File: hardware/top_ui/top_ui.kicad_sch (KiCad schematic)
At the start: 24 parts, among them J1 USB-C, J2 J_STK_A, J3 J_STK_B, J5 ST77916 QSPI, J6 Stern, J7 Radar, Q1 BC847, Q2 P-FET 20V 1A, SW1A BTN1, SW1B BTN1, SW2A BTN2, SW2B BTN2, SW3A BTN3, SW3B BTN3, SW4A BTN4, SW4B BTN4, U1 USBLC6-2SC6, U2 SHT40-AD1B

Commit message: feat: Layouts aller drei Boards - platziert, vernetzt, DRC-sauber
Neuer Generator tools/gen_layouts.py erzeugt die drei .kicad_pcb komplett:
Outline, Bohrbild, Frontmarkierung, Antennen-Sperrflaeche, alle Footprints
mit Netzen aus den Schaltplan-Generatoren, PGND-Zonen beidseitig. Mechanisch
gebundene Teile exakt platziert (Stackverbinder deckungsgleich, Taster auf
den Sichel-Stoesselpositionen, USB-C am Rand, ESP32-Antenne an der
Frontkante, FET-Raster berechnet); Rest kollisionsfrei per Spiralsuche mit
Netznachbar-Heuristik. DRC (pcbnew.WriteDRCReport - kicad-cli kann das erst
ab KiCad 8): KEINE Platzierungsfehler auf allen drei Boards. Offen bleibt
das ROUTING - die Boards sind route-fertig, Leiterbahnen sind Handarbeit.

Die Kollisionspruefung fand einen echten Mechanikfehler: Bohrbild v2.
Die Bohrungen 120/240 Grad lagen ~2 mm neben den Sicheltasten-Stoesseln
(117/243) - Schraubenkopf trifft Taster. Auf r21,5 blockieren Stack-
verbinder, ESP32-Antenne und Leistungsstecker alle uebrigen Winkel; frei
sind exakt 0/180. Jetzt zwei Schrauben, Verdrehsicherung ueber die beiden
Stackverbinder. docs/04 und gen_boards nachgezogen.

Weitere Ausbeute der Iterationen (jede von DRC oder Kollisionspruefung
erzwungen): Stackverbinder auf x=+/-14,2 (Diagonaltaster!), Taster auf
Alps-SKRK-Footprint (EVQP2-Pads ragten 0,1 mm an den Rand), Rotations-
automatik fuer die Taster nach minimalem Pad-Radius, Sicherung auf
SMD-NANO2, Bulk-Elkos niedrigbauend auf die Rueckseite, Treiber gestaffelt
unter den FETs, HSOP ohne Thermal-Vias (0,2-mm-Bohrungen), Flip-Bug der
Autoplatzierung (Teile blieben nach B-Versuch gespiegelt), Segfault-
Workarounds fuer ZONE_FILLER und BOX2-Merge in der headless pcbnew-API.

Schaltplan-Nebenkorrekturen: L78L12-Pinbelegung war verdreht (1=OUT!),
Q1-Verpolschutz auf PowerPAK mit eigener Pad-Zuordnung, SHT4x-Footprint
lag in Sensor_Humidity statt Package_DFN_QFN.

USB-C-Randverletzungen (10) sind als Steckerueberhang beabsichtigt und
werden getrennt ausgewie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
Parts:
- SW1A, SW1B, SW2A, SW2B, SW3A, SW3B, SW4A, SW4B: footprint Button_Switch_SMD:SW_SPST_EVQP2 -> Button_Switch_SMD:SW_Push_SPST_NO_Alps_SKRK; MPN niedrig, 3,9x2,9 - Position siehe mechanical/frontplate.py -> Alps SKRK o.ae., 3,9x2,9, Pads laengs - Position siehe mech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
- U2: footprint Package_DFN_QFN:DFN-4-1EP_1.5x1.5mm_P0.8mm_EP0.7x0.9mm -> Sensor_Humidity:Sensirion_DFN-4_1.5x1.5mm_P0.8mm_SHT4x_NoCentralPad
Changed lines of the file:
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@@
     (property "Value" "BTN1" (at 234.9500 20.3200 0)
       (effects (font (size 1.27 1.27)) (justify left)))
-    (property "Footprint" "Button_Switch_SMD:SW_SPST_EVQP2" (at 228.6000 25.4000 0)
+    (property "Footprint" "Button_Switch_SMD:SW_Push_SPST_NO_Alps_SKRK" (at 228.6000 25.4000 0)
       (effects (font (size 1.27 1.27)) hide))
-    (property "MPN" "niedrig, 3,9x2,9 - Position siehe mechanical/frontplate.py" (at 228.6000 27.9400 0)
+    (property "MPN" "Alps SKRK o.ae., 3,9x2,9, Pads laengs - Position siehe mechanical/frontplate.py" (at 228.6000 27.9400 0)
       (effects (font (size 1.27 1.27)) hide))
     (pin "1")
@@
     (property "Value" "BTN1" (at 285.7500 20.3200 0)
       (effects (font (size 1.27 1.27)) (justify left)))
-    (property "Footprint" "Button_Switch_SMD:SW_SPST_EVQP2" (at 279.4000 25.4000 0)
+    (property "Footprint" "Button_Switch_SMD:SW_Push_SPST_NO_Alps_SKRK" (at 279.4000 25.4000 0)
       (effects (font (size 1.27 1.27)) hide))
-    (property "MPN" "niedrig, 3,9x2,9 - Position siehe mechanical/frontplate.py" (at 279.4000 27.9400 0)
+    (property "MPN" "Alps SKRK o.ae., 3,9x2,9, Pads laengs - Position siehe mechanical/frontplate.py" (at 279.4000 27.9400 0)
       (effects (font (size 1.27 1.27)) hide))
     (pin "1")
@@
     (property "Value" "BTN2" (at 336.5500 20.3200 0)
       (effects (font (size 1.27 1.27)) (justify left)))
-    (property "Footprint" "Button_Switch_SMD:SW_SPST_EVQP2" (at 330.2000 25.4000 0)
+    (property "Footprint" "Button_Switch_SMD:SW_Push_SPST_NO_Alps_SKRK" (at 330.2000 25.4000 0)
       (effects (font (size 1.27 1.27)) hide))
-    (property "MPN" "niedrig, 3,9x2,9 - Position siehe mechanical/frontplate.py" (at 330.2000 27.9400 0)
+    (property "MPN" "Alps SKRK o.ae., 3,9x2,9, Pads laengs - Position siehe mechanical/frontplate.py" (at 330.2000 27.9400 0)
       (effects (font (size 1.27 1.27)) hide))
     (pin "1")
@@
     (property "Value" "BTN2" (at 387.3500 20.3200 0)
       (effects (font (size 1.27 1.27)) (justify left)))
-    (property "Footprint" "Button_Switch_SMD:SW_SPST_EVQP2" (at 381.0000 25.4000 0)
+    (property "Footprint" "Button_Switch_SMD:SW_Push_SPST_NO_Alps_SKRK" (at 381.0000 25.4000 0)
       (effects (font (size 1.27 1.27)) hide))
-    (property "MPN" "niedrig, 3,9x2,9 - Position siehe mechanical/frontplate.py" (at 381.0000 27.9400 0)
+    (property "MPN" "Alps SKRK o.ae., 3,9x2,9, Pads laengs - Position siehe mechanical/frontplate.py" (at 381.0000 27.9400 0)
       (effects (font (size 1.27 1.27)) hide))
     (pin "1")
@@
     (property "Value" "BTN3" (at 438.1500 20.3200 0)
       (effects (font (size 1.27 1.27)) (justify left)))
-    (property "Footprint" "Button_Switch_SMD:SW_SPST_EVQP2" (at 431.8000 25.4000 0)
+    (property "Footprint" "Button_Switch_SMD:SW_Push_SPST_NO_Alps_SKRK" (at 431.8000 25.4000 0)
       (effects (font (size 1.27 1.27)) hide))
-    (property "MPN" "niedrig, 3,9x2,9 - Position siehe mechanical/frontplate.py" (at 431.8000 27.9400 0)
+    (property "MPN" "Alps SKRK o.ae., 3,9x2,9, Pads laengs - Position siehe mechanical/frontplate.py" (at 431.8000 27.9400 0)
       (effects (font (size 1.27 1.27)) hide))
     (pin "1")
@@
     (property "Value" "BTN3" (at 31.7500 64.7700 0)
       (effects (font (size 1.27 1.27)) (justify left)))
-    (property "Footprint" "Button_Switch_SMD:SW_SPST_EVQP2" (at 25.4000 69.8500 0)
+    (property "Footprint" "Button_Switch_SMD:SW_Push_SPST_NO_Alps_SKRK" (at 25.4000 69.8500 0)
       (effects (font (size 1.27 1.27)) hide))
-    (property "MPN" "niedrig, 3,9x2,9 - Position siehe mechanical/frontplate.py" (at 25.4000 72.3900 0)
+    (property "MPN" "Alps SKRK o.ae., 3,9x2,9, Pads laengs - Position siehe mechanical/frontplate.py" (at 25.4000 72.3900 0)
       (effects (font (size 1.27 1.27)) hide))
     (pin "1")
@@
     (property "Value" "BTN4" (at 82.5500 64.7700 0)
       (effects (font (size 1.27 1.27)) (justify left)))
-    (property "Footprint" "Button_Switch_SMD:SW_SPST_EVQP2" (at 76.2000 69.8500 0)
+    (property "Footprint" "Button_Switch_SMD:SW_Push_SPST_NO_Alps_SKRK" (at 76.2000 69.8500 0)
       (effects (font (size 1.27 1.27)) hide))
-    (property "MPN" "niedrig, 3,9x2,9 - Position siehe mechanical/frontplate.py" (at 76.2000 72.3900 0)
+    (property "MPN" "Alps SKRK o.ae., 3,9x2,9, Pads laengs - Position siehe mechanical/frontplate.py" (at 76.2000 72.3900 0)
       (effects (font (size 1.27 1.27)) hide))
     (pin "1")
@@
     (property "Value" "BTN4" (at 133.3500 64.7700 0)
       (effects (font (size 1.27 1.27)) (justify left)))
-    (property "Footprint" "Button_Switch_SMD:SW_SPST_EVQP2" (at 127.0000 69.8500 0)
+    (property "Footprint" "Button_Switch_SMD:SW_Push_SPST_NO_Alps_SKRK" (at 127.0000 69.8500 0)
       (effects (font (size 1.27 1.27)) hide))
-    (property "MPN" "niedrig, 3,9x2,9 - Position siehe mechanical/frontplate.py" (at 127.0000 72.3900 0)
+    (property "MPN" "Alps SKRK o.ae., 3,9x2,9, Pads laengs - Position siehe mechanical/frontplate.py" (at 127.0000 72.3900 0)
       (effects (font (size 1.27 1.27)) hide))
     (pin "1")
@@
     (property "Value" "SHT40-AD1B" (at 184.1500 64.7700 0)
       (effects (font (size 1.27 1.27)) (justify left)))
-    (property "Footprint" "Package_DFN_QFN:DFN-4-1EP_1.5x1.5mm_P0.8mm_EP0.7x0.9mm" (at 177.8000 69.8500 0)
+    (property "Footprint" "Sensor_Humidity:Sensirion_DFN-4_1.5x1.5mm_P0.8mm_SHT4x_NoCentralPad" (at 177.8000 69.8500 0)
       (effects (font (size 1.27 1.27)) hide))
     (property "MPN" "Adresse 0x44 - muss zur YAML passen; thermisch vom Board entkoppeln (Schlitze)" (at 177.8000 72.3900 0)

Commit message: Reed-Kontakte, Haubenkontakt, Klinkenbuchse, ToF statt Radar
Funktional neu
--------------
- Zwei Reed-Eingaenge fuer Fensterkontakte auf den einzigen noch freien
  Expanderpins P6/P7. 10k Pullup, 1k Serie, 100n und TVS je Kanal; bei
  geschlossenem Kontakt liegen 0,3 V am PCF8574, sicher unter VIL.
- Meldekontakt zur Dunstabzugshaube ueber PhotoMOS AQY282GS statt Relais:
  potentialfrei, 60 V / 0,8 A, kein Spulenstrom, keine Bauhoehe im 9-mm-
  Stapelspalt. NUR SELV - bei 230 V gehoert das Schaltglied nicht in die Dose.
- Weihnachtsstern jetzt gesteckt: Klinkenbuchse im oberen Steg der
  Frontplatte, PTC 0,2 A direkt an der Buchse gegen den Kurzschluss beim
  Stecken, Bulk vor die Sicherung gelegt.
- Radar durch VL53L1X (ToF) ersetzt. Hinter dieser Frontplatte hat kein
  20-mm-Radarmodul freie Sicht; der ToF passt als 4,9 x 2,5 mm grosser Chip
  in den Steg. Er misst Entfernung statt Empfindlichkeit - Schwelle exakt
  1 m - und deckt in der Fensterlaibung zugleich den Durchstieg ab.
  Netze umbenannt: RADAR_INT -> PRESENCE_INT, UART_RADAR_* -> UART_AUX_*.
  J7 bleibt unbestueckt als Reserve, damit das Stackpinout unberuehrt bleibt.

Frontplatte
-----------
Oberer Steg 9 -> 17 mm, damit Klinkenbuchse und ToF-Fenster nebeneinander
passen; Sicheln dadurch ~70 -> ~45 Grad, Stoesselwinkel 18 -> 12 Grad.
ToF-Kanal konisch (4,5 vorn, 3,0 hinten) fuer den Sichtkegel. Kabelausgang
Ø4,5 entfaellt. Selbsttests bestanden, STEP/STL neu erzeugt.

KiCad 10
--------
Die Generatoren liefen nur gegen KiCad-9-Bibliotheken. Migriert:
- Symbol- und Footprintpfad werden gefunden (Linux, macOS, Umgebungsvariable)
- PCF8574 -> PCF8574T (pinkompatibel, als Alias)
- Q_NMOS_GDS/Q_PMOS_GSD/Q_NPN_BCE liegen jetzt als hardware/lib/
  SwitchStack.kicad_sym im Projekt. KiCad 10 nummeriert die Stockvarianten
  mit G/D/S bzw. B/C/E - ein Alias haette die Anschluesse still vertauscht.
- USB-C-Schirm heisst SH statt S1, Zonen-API SetDoNotAllowZoneFills,
  DRC laeuft ueber kicad-cli statt WriteDRCRepo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
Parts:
- added C3: 100n, Capacitor_SMD:C_0603_1608Metric, symbol Device:C
- added C4: 4u7, Capacitor_SMD:C_0603_1608Metric, symbol Device:C
- added F1: 0,2 A PTC, Fuse:Fuse_1206_3216Metric, symbol Device:Polyfuse
- added R5: 10k, Resistor_SMD:R_0603_1608Metric, symbol Device:R
- added U3: VL53L1X, Sensor_Distance:ST_VL53L1x, symbol Sensor_Distance:VL53L1CXV0FY1
- J6: value Stern -> Stern Klinke; footprint Connector_JST:JST_PH_B2B-PH-K_1x02_P2.00mm_Vertical -> Connector_Audio:Jack_3.5mm_QingPu_WQP-PJ398SM_Vertical_CircularHoles; symbol Connector_Generic:Conn_01x02 -> Connector_Audio:AudioJack2_SwitchT; MPN Kabel durch den Frontplatten-Ausgang Ø4,5 -> PLATZHALTER 3,5 mm vertikal - Zielteil 2,5 mm, Bauhoehe max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
- J7: value Radar -> Reserve UART; MPN Belegung an reales Modul anpassen (offener Punkt 17) -> DNP - Reserve fuer ein Satellitenmodul
- Q1: symbol Device:Q_NPN_BCE -> SwitchStack:Q_NPN_BCE
- Q2: symbol Device:Q_PMOS_GSD -> SwitchStack:Q_PMOS_GSD
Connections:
- net 3V3_SYS: now also C3.1, C4.1, R5.1, U3.1 (AVDDVCSEL), U3.11 (AVDD)
- net I2C_SCL: now also U3.10 (SCL)
- net I2C_SDA: now also U3.9 (SDA)
- net PGND: now also J1.SH (SHIELD), J6.S, C3.2, C4.2, U3.12 (GND), U3.2 (AVSSVCSEL), U3.3 (GND), U3.4 (GND), U3.6 (GND); no longer J1.S1 (SHIELD), J6.2 (Pin_2)
- net STAR_OUT: now also J6.T, F1.2; no longer C2.1, J6.1 (Pin_1)
- net RADAR_INT renamed PRESENCE_INT
- net PRESENCE_INT: now also U3.7 (GPIO1)
- net UART_RADAR_RX renamed UART_AUX_RX
- net UART_RADAR_TX renamed UART_AUX_TX
- new net STAR_SW: C2.1, F1.1
- new net TOF_XSHUT: R5.2, U3.5 (XSHUT)
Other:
- moved on the sheet: J2, J3, J7

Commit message: Weg A umgesetzt: Top-Board quadratisch, vier Ecktaster unter den Kreuzen
Umriss
------
gen_layouts.py und gen_boards.py kennen jetzt eine zweite Kontur. Das Top-Board
ist ein abgerundetes Quadrat, 49 x 49 mm mit Eckradius 4 - vier Geraden und vier
Boegen auf Edge.Cuts. Mid und Bottom bleiben rund und unangetastet; ihre
Boarddateien wurden nicht angefasst, die 985 Leiterbahnen des Bottom-Boards sind
unberuehrt.

Kantenmitte 24,5 liegt 0,5 mm innerhalb der Rastnasenlinie der Zentralscheibe
(50,0). Der Konturtest der Platzierung (inside_outline) rechnet die abgerundeten
Ecken korrekt mit, sonst haette die Automatik die Ecken verschenkt.

Taster
------
Acht parallelgeschaltete Sicheltaster werden vier Ecktaster, exakt auf
(+/-18,0 / +/-20,0) - den gemessenen Druckkreuzen der Scheibe. Ein Kreuz ist
3,2 mm gross und trifft genau einen Taster; parallelschalten waere sinnlos.
Der Schaltplan ist entsprechend neu erzeugt (25 statt 29 Bauteile,
Netzlistenvergleich bestanden), die Stuecklisten ebenfalls.

Durchbrueche
------------
Die vier Oeffnungen der Scheibe liegen jetzt bei (+/-9 / +/-19) - in den
Diagonalfeldern zwischen Pfeil und Ecktaster, mit rund 8 mm Abstand zu beiden.
Auf den Diagonalen selbst ist kein Platz mehr, dort sitzen die Kreuze. Links
oben ToF, links unten Klinke, rechts zweimal Lueftung - und weil dort die Luft
hereinkommt, sitzt der SHT4x jetzt unter dem oberen rechten Schlitz (Punkt 46).

Ergebnis: Platzierung kollisionsfrei, DRC unveraendert 28 clearance (die
bekannten Pad-Abstaende im USB-C-Footprint) plus die eine Randverletzung des
Klinken-Platzhalters.

Was dabei aufgefallen ist
-------------------------
gen_boards.py ueberschreibt hardware/<slug>/<slug>.kicad_pcb - es haette beim
naechsten Lauf die Bestueckung UND die Leiterbahnen aller drei Boards
weggeworfen. Das steht jetzt als Warnung im Docstring.

Der Fertigungsnutzen ist geloescht: gen_panel.py setzt drei Kreise Oe52
nebeneinander und wuerde um das quadratische Board eine runde Fraesbahn leg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
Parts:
- removed SW1A, SW1B: BTN1, Button_Switch_SMD:SW_Push_SPST_NO_Alps_SKRK, symbol Switch:SW_Push
- removed SW2A, SW2B: BTN2, Button_Switch_SMD:SW_Push_SPST_NO_Alps_SKRK, symbol Switch:SW_Push
- removed SW3A, SW3B: BTN3, Button_Switch_SMD:SW_Push_SPST_NO_Alps_SKRK, symbol Switch:SW_Push
- removed SW4A, SW4B: BTN4, Button_Switch_SMD:SW_Push_SPST_NO_Alps_SKRK, symbol Switch:SW_Push
- added SW1: BTN1, Button_Switch_SMD:SW_Push_SPST_NO_Alps_SKRK, symbol Switch:SW_Push
- added SW2: BTN2, Button_Switch_SMD:SW_Push_SPST_NO_Alps_SKRK, symbol Switch:SW_Push
- added SW3: BTN3, Button_Switch_SMD:SW_Push_SPST_NO_Alps_SKRK, symbol Switch:SW_Push
- added SW4: BTN4, Button_Switch_SMD:SW_Push_SPST_NO_Alps_SKRK, symbol Switch:SW_Push
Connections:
- net BTN1: now also SW1.1
- net BTN2: now also SW2.1
- net BTN3: now also SW3.1
- net BTN4: now also SW4.1
- net PGND: now also SW1.2, SW2.2, SW3.2, SW4.2
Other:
- moved on the sheet: C1, C2, C3, C4, F1, J2, J3, J5, J6, J7, Q1, Q2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

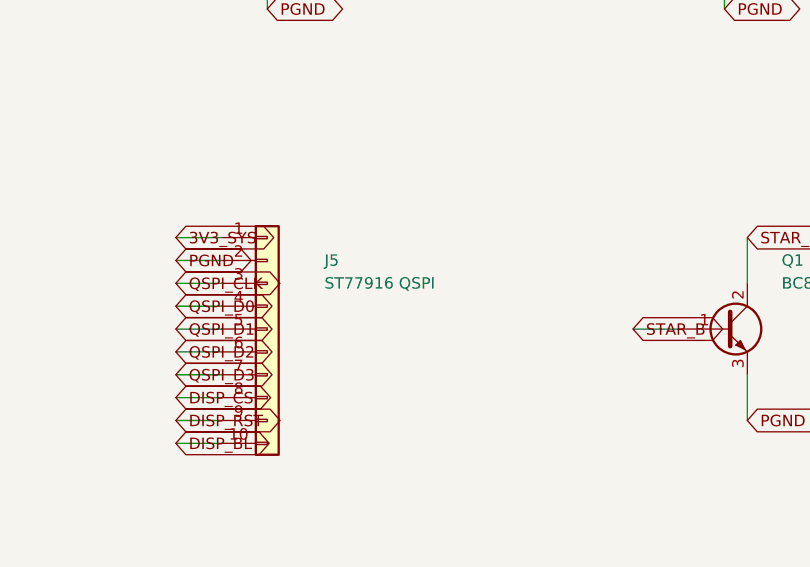
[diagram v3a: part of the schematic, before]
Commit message: Display auf ST7789 240x280 umgestellt; Tastenpaare in der Firmware aufgeloest
Display
-------
Der Fensterausschnitt der Zentralscheibe misst gemessene 32,70 x 27,00 mm. Die
aktive Flaeche eines 1,69-Zoll-Panels mit 240x280 ist quer eingebaut
32,63 x 27,97 - in der Breite bleiben 0,07 mm, in der Hoehe verdeckt das Fenster
einen halben Millimeter je Seite. Damit ist Punkt 43 entschieden.

Der Gewinn liegt nicht in der Groesse, sondern im Treiber: ESPHome kennt den
ST7789 nativ. st77916_init.yaml mit seinen 214 Herstellerkommandos ist geloescht.

Die Netznamen am Stack bleiben QSPI_*, obwohl der ST7789 4-Draht-SPI ist. Sie
laufen ueber J_STK_B durch alle drei Boards, und eine Umbenennung wuerde auch
den Bottom-Schaltplan aendern - dessen Layout traegt 985 Leiterbahnen. Die
Belegung steht stattdessen als Kommentar an beiden Stellen: QSPI_CLK = SCK,
QSPI_D0 = MOSI, QSPI_D1 = DC, D2/D3 frei.

Tastenpaare
-----------
Die vier Ecktaster heissen in der Konfiguration jetzt ecke_ol/or/ul/ur und sind
intern - einzeln bedeuten sie nichts. Darueber liegen vier Template-Sensoren,
die die Paare aufloesen: hoch = ol+or, runter = ul+ur, OK = or+ur, play = ol+ul.
30 ms Verzoegerung fangen ab, dass die beiden Taster eines Paares nie exakt
gleichzeitig schliessen.

Die Zuordnung Richtung -> Aktion ist vorlaeufig (hoch/runter fahren beide
Jalousien, OK stoppt, play liegt brach). Verbindlich wird sie erst mit der
Menue-Zustandsmaschine, Punkt 37.

Ehrlich dazu
------------
Die Konfiguration ist NICHT mit `esphome config` geprueft - auf diesem Rechner
ist ESPHome nicht installiert. Sie parst als YAML, mehr ist nicht gezeigt.
Besonders die Panel-Offsets (0/20) und die Template-Lambdas gehoeren vor dem
ersten Flash validiert. Der Hinweis steht in der Datei selbst, in
firmware/README, in der README und in docs/13.

Co-Authored-By: Claude Opus 5 (1M context) <noreply@anthropic.com>
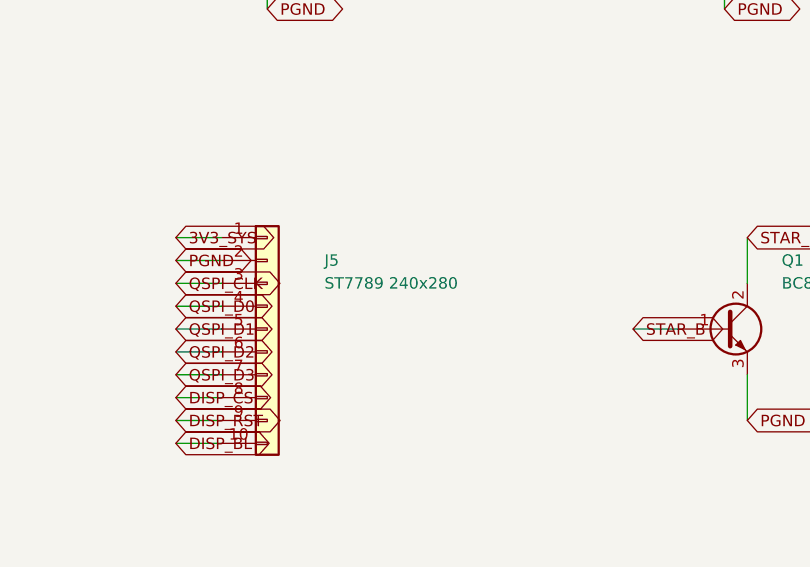
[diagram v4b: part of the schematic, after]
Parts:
- J5: value ST77916 QSPI -> ST7789 240x280; MPN PLATZHALTER - reales Modul-FPC vermessen, dann Footprint ta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 -> PLATZHALTER - reales Modul mit FPC vermessen, dann Footprin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
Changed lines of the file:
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@@
     (property "Reference" "J5" (at 82.5500 62.2300 0)
       (effects (font (size 1.27 1.27)) (justify left)))
-    (property "Value" "ST77916 QSPI" (at 82.5500 64.7700 0)
+    (property "Value" "ST7789 240x280" (at 82.5500 64.7700 0)
       (effects (font (size 1.27 1.27)) (justify left)))
     (property "Footprint" "Connector_PinHeader_1.27mm:PinHeader_1x10_P1.27mm_Vertical" (at 76.2000 69.8500 0)
       (effects (font (size 1.27 1.27)) hide))
-    (property "MPN" "PLATZHALTER - reales Modul-FPC vermessen, dann Footprint tauschen" (at 76.2000 72.3900 0)
+    (property "MPN" "PLATZHALTER - reales Modul mit FPC vermessen, dann Footprint und Pinzahl tauschen (Module haben meist 8 Pins)" (at 76.2000 72.3900 0)
       (effects (font (size 1.27 1.27)) hide))
     (pin "1")

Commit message: Stehende USB-C-Buchse, Nutzen mit gemischter Geometrie - Top ist DRC-sauber
USB-C (Punkt 45)
----------------
Gewaehlt: G-Switch GT-USB-7051x, vertikal SMT, 22 Pads (A- und B-Reihe
vollstaendig, also steckrichtungsunabhaengig), Footprint 9,94 x 6,40 mm,
LCSC C2843970. Sie sitzt mittig oben, zeigt nach vorn und liegt unter der
Zentralscheibe - erreichbar erst nach deren Abnahme, so wie es Punkt 45
verlangt.

Der Nebeneffekt ist der eigentliche Gewinn: Die 28 clearance-Meldungen, die das
Top-Board seit dem ersten Layout begleitet haben, sind verschwunden. Sie waren
nie ein Layoutfehler, sondern die zu eng gerasterten Pads der liegenden GCT
USB4085 gegen unsere 0,15-mm-Vorgabe. Das Top-Board meldet jetzt KEINEN
DRC-Fehler mehr - nur noch drei bewusste Randverletzungen (zwei davon sind die
NPTH-Loecher der Buchse gegen ihre eigenen Pads, eine der Klinken-Platzhalter).

Der Waiver-Mechanismus in gen_layouts.py war dafuer zu grob: Er hat nur auf das
Zeilenende geprueft. Jetzt wird nur gewaivert, wenn ALLE in der Meldung
genannten Bauteile in der Ausnahmeliste stehen - sonst verschluckt ein Waiver
fuer J1 auch eine echte Kollision J1 gegen U3.

Fertigungsnutzen
----------------
gen_panel.py beherrscht gemischte Geometrie: zwei Kreise Oe52 und ein
abgerundetes Quadrat 47 x 47. Das Quadrat bekommt seine Fraesfuge als
Parallelkurve der Kontur, mit vier Stegen - je einer pro Kante, um 10 mm aus der
Mitte versetzt, weil dort entweder eine Befestigungsbohrung oder der
ueberstehende Klinken-Platzhalter sitzt. 173,4 x 64,4 mm = 112 cm2.

Zwei Fehler dabei gefunden und behoben: Die geschlossene Konturliste endete auf
ihrem eigenen Anfangspunkt - beim Umlauf entstand ein Segment der Laenge null,
und KiCad meldete die ganze Kontur als ungueltig. Und die Seitennamen der Stege
sind KiCad-Koordinaten mit y nach unten; die erste Fassung setzte den Steg
deshalb genau auf die Klinke.

Der DRC des Nutzens ist wieder deckungsgleich mit der Summe der Einzelboards.

Co-Authored-By: Claude Opus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
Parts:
- J1: footprint Connector_USB:USB_C_Receptacle_GCT_USB4085 -> Connector_USB:USB_C_Receptacle_G-Switch_GT-USB-7051x; MPN 16-Pin-Typ, nur USB 2.0 -> G-Switch GT-USB-7051A/B, vertikal SMT (LCSC C2843970) - Bau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
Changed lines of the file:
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@@
     (property "Value" "USB-C" (at 31.7500 20.3200 0)
       (effects (font (size 1.27 1.27)) (justify left)))
-    (property "Footprint" "Connector_USB:USB_C_Receptacle_GCT_USB4085" (at 25.4000 25.4000 0)
+    (property "Footprint" "Connector_USB:USB_C_Receptacle_G-Switch_GT-USB-7051x" (at 25.4000 25.4000 0)
       (effects (font (size 1.27 1.27)) hide))
-    (property "MPN" "16-Pin-Typ, nur USB 2.0" (at 25.4000 27.9400 0)
+    (property "MPN" "G-Switch GT-USB-7051A/B, vertikal SMT (LCSC C2843970) - Bauhoehe gegen die 4,5 mm bis zur Scheibe pruefen" (at 25.4000 27.9400 0)
       (effects (font (size 1.27 1.27)) hide))
     (pin "A1")
